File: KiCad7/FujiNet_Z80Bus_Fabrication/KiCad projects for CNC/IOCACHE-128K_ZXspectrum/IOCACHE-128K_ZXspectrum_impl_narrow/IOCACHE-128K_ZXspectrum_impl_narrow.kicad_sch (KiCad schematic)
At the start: 0 parts

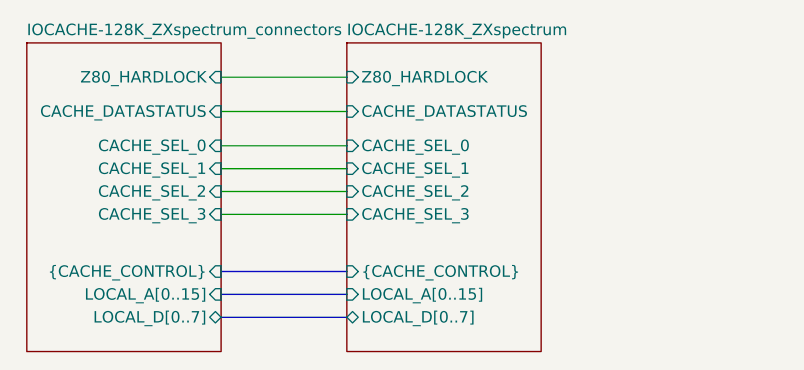
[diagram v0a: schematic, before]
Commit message: KICAD IOCACHE fixed
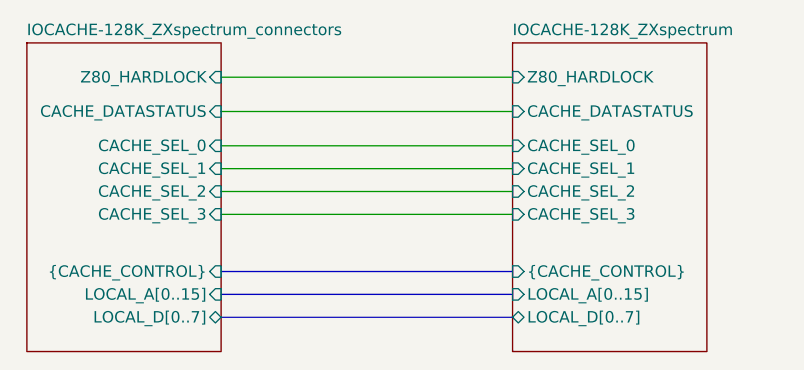
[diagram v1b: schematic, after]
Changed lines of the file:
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@@
   )
   (bus_alias "Z80_CONTROL" (members "Z80_CONTROL.RD" "Z80_CONTROL.WR" "Z80_CONTROL.IORQ" "Z80_CONTROL.MEMRQ" "Z80_CONTROL.BUSRQ" "Z80_CONTROL.WAIT" "Z80_CONTROL.ROMCS" "Z80_CONTROL.BUSACK" "Z80_CONTROL.NMI" "Z80_CONTROL.RESET"))
-  (wire (pts (xy 81.28 66.04) (xy 95.25 66.04))
+  (wire (pts (xy 81.28 66.04) (xy 113.665 66.04))
     (stroke (width 0) (type default))
   )
-  (bus (pts (xy 81.28 77.47) (xy 95.25 77.47))
+  (bus (pts (xy 81.28 77.47) (xy 113.665 77.47))
     (stroke (width 0) (type default))
   )
-  (wire (pts (xy 81.28 60.96) (xy 95.25 60.96))
+  (wire (pts (xy 81.28 60.96) (xy 113.665 60.96))
     (stroke (width 0) (type default))
   )
-  (wire (pts (xy 81.28 50.8) (xy 95.25 50.8))
+  (wire (pts (xy 81.28 50.8) (xy 113.665 50.8))
     (stroke (width 0) (type default))
   )
-  (wire (pts (xy 81.28 58.42) (xy 95.25 58.42))
+  (wire (pts (xy 81.28 58.42) (xy 113.665 58.42))
     (stroke (width 0) (type default))
   )
-  (wire (pts (xy 81.28 63.5) (xy 95.25 63.5))
+  (wire (pts (xy 81.28 63.5) (xy 113.665 63.5))
     (stroke (width 0) (type default))
   )
-  (bus (pts (xy 81.28 74.93) (xy 95.25 74.93))
+  (bus (pts (xy 81.28 74.93) (xy 113.665 74.93))
     (stroke (width 0) (type default))
   )
-  (bus (pts (xy 81.28 72.39) (xy 95.25 72.39))
+  (bus (pts (xy 81.28 72.39) (xy 113.665 72.39))
     (stroke (width 0) (type default))
   )
-  (wire (pts (xy 81.28 54.61) (xy 95.25 54.61))
+  (wire (pts (xy 81.28 54.61) (xy 113.665 54.61))
     (stroke (width 0) (type default))
   )
-  (sheet (at 95.25 46.99) (size 21.59 34.29) (fields_autoplaced)
+  (sheet (at 113.665 46.99) (size 21.59 34.29) (fields_autoplaced)
     (stroke (width 0.1524) (type solid))
     (fill (color 0 0 0 0.0000))
-    (property "Sheetname" "IOCACHE-128K_ZXspectrum" (at 95.25 46.2784 0)
+    (property "Sheetname" "IOCACHE-128K_ZXspectrum" (at 113.665 46.2784 0)
       (effects (font (size 1.27 1.27)) (justify left bottom))
     )
-    (property "Sheetfile" "../IOCACHE-128K_ZXspectrum.kicad_sch" (at 95.25 81.8646 0)
+    (property "Sheetfile" "../IOCACHE-128K_ZXspectrum.kicad_sch" (at 113.665 81.8646 0)
       (effects (font (size 1.27 1.27)) (justify left top) hide)
     )
-    (pin "Z80_HARDLOCK" input (at 95.25 50.8 180)
+    (pin "Z80_HARDLOCK" input (at 113.665 50.8 180)
       (effects (font (size 1.27 1.27)) (justify left))
     )
-    (pin "CACHE_DATASTATUS" input (at 95.25 54.61 180)
+    (pin "CACHE_DATASTATUS" input (at 113.665 54.61 180)
       (effects (font (size 1.27 1.27)) (justify left))
     )
-    (pin "{CACHE_CONTROL}" input (at 95.25 72.39 180)
+    (pin "{CACHE_CONTROL}" input (at 113.665 72.39 180)
       (effects (font (size 1.27 1.27)) (justify left))
     )
-    (pin "CACHE_SEL_1" input (at 95.25 60.96 180)
+    (pin "CACHE_SEL_1" input (at 113.665 60.96 180)
       (effects (font (size 1.27 1.27)) (justify left))
     )
-    (pin "CACHE_SEL_3" input (at 95.25 66.04 180)
+    (pin "CACHE_SEL_3" input (at 113.665 66.04 180)
       (effects (font (size 1.27 1.27)) (justify left))
     )
-    (pin "CACHE_SEL_2" input (at 95.25 63.5 180)
+    (pin "CACHE_SEL_2" input (at 113.665 63.5 180)
       (effects (font (size 1.27 1.27)) (justify left))
     )
-    (pin "CACHE_SEL_0" input (at 95.25 58.42 180)
+    (pin "CACHE_SEL_0" input (at 113.665 58.42 180)
       (effects (font (size 1.27 1.27)) (justify left))
     )
-    (pin "LOCAL_D[0..7]" bidirectional (at 95.25 77.47 180)
+    (pin "LOCAL_D[0..7]" bidirectional (at 113.665 77.47 180)
       (effects (font (size 1.27 1.27)) (justify left))
     )
-    (pin "LOCAL_A[0..15]" input (at 95.25 74.93 180)
+    (pin "LOCAL_A[0..15]" input (at 113.665 74.93 180)
       (effects (font (size 1.27 1.27)) (justify left))
     )
